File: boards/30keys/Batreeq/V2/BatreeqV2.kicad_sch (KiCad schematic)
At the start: 103 parts, among them J1 Conn_01x12_Female, J2 Conn_01x12_Female, SW1 SW_Push, SW10 SW_Push, SW11 SW_Push, SW12 SW_Push, SW13 SW_Push, SW14 SW_Push, SW15 SW_Push, SW16 SW_Push, SW17 SW_Push, SW18 SW_Push, SW19 SW_Push, SW2 SW_Push, SW20 SW_Push, SW21 SW_Push, SW22 SW_Push, SW23 SW_Push, SW24 SW_Push, SW25 SW_Push, SW26 SW_Push, SW27 SW_Push, SW28 SW_Push, SW29 SW_Push, SW3 SW_Push, SW30 SW_Push, SW31 SW_Push, SW32 SW_Push, SW33 SW_Push, SW34 SW_Push, SW35 SW_Push, SW36 RotaryEncoder, SW37 SW_SPDT, SW4 SW_Push, SW5 SW_Push, SW6 SW_Push, SW7 SW_Push, SW8 SW_Push, SW9 SW_Push, U1 Elite-C, U2 74HC595, U3 TCR2EF19,LM(CT, U4 PMW3360DM-T2QU, U5 DRV2605L

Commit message: batreeqv2
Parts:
- added C6: 4u7, Capacitor_SMD:C_0402_1005Metric, symbol Device:C
- added D40: B5817WS, josh-passives-smt:D_SOD-323, symbol Device:D_Schottky
- added D41, D42, D43, D44, D45, D46, D47, D48, D49, D50, D51, D52, D53, D54, D55, D56, D57, D58, D59, D60, D61, D62, D63, D64, D65, D66, D67, D68, D69, D70, D71, D72, D73, D74: SK6812MINI-E, Alaa:MX_SK6812MINI-E_REV, symbol kicad-keyboard-parts:SK6812MINI-E
- added F1: 500mA, josh-passives-smt:Fuse_0603_1608Metric, symbol Device:Polyfuse_Small
- added J4: Conn_01x08_Female, Alaa:3JST_BAT, symbol Connector:Conn_01x03_Female
- added JP1, JP2, JP3, JP4, JP5, JP6: Jumper_2_Open, Jumper:SolderJumper-2_P1.3mm_Open_TrianglePad1.0x1.5mm, symbol Jumper:Jumper_2_Open
- added U6: 74LVC1T45, josh-soic-sot-etc:SOT-563, symbol Logic_LevelTranslator:SN74LVC1T45DRL
- D1, D10, D11, D12, D13, D14, D15, D16, D17, D18, D19, D2, D20, D21, D22, D23, D24, D25, D26, D27, D28, D29, D3, D30, D31, D32, D33, D34, D35, D36, D37, D38, D39, D4, D5, D6, D7, D8, D9: LCSC C909967 -> C8598
- J3: value (none) -> Conn_01x08_Female; footprint (none) -> Connector_JST:JST_PH_S8B-PH-K_1x08_P2.00mm_Horizontal
- SW1, SW10, SW11, SW12, SW13, SW14, SW15, SW16, SW17, SW18, SW19, SW2, SW20, SW21, SW22, SW23, SW24, SW25, SW26, SW27, SW28, SW29, SW3, SW30, SW31, SW32, SW33, SW34, SW4, SW5, SW6, SW7, SW8, SW9: footprint Alaa:Kailh_hotswap_MX-CHOC-connected -> Alaa:Kailh_hotswap_only_MX-CHOC
- U1: value Elite-C -> (none); footprint Alaa:Elite-C-N!N -> (none); symbol alaa:Elite-C -> alaa:Helios_SeaPicro
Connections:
- net GND: now also C6.2, D41.3 (VSS), D42.3 (VSS), D43.3 (VSS), D44.3 (VSS), D45.3 (VSS), D46.3 (VSS), D47.3 (VSS), D48.3 (VSS), D49.3 (VSS), D50.3 (VSS), D51.3 (VSS), D52.3 (VSS), D53.3 (VSS), D54.3 (VSS), D55.3 (VSS), D56.3 (VSS), D57.3 (VSS), D58.3 (VSS), D59.3 (VSS), D60.3 (VSS), D61.3 (VSS), D62.3 (VSS), D63.3 (VSS), D64.3 (VSS), D65.3 (VSS), D66.3 (VSS), D67.3 (VSS), D68.3 (VSS), D69.3 (VSS), D70.3 (VSS), D71.3 (VSS), D72.3 (VSS), D73.3 (VSS), D74.3 (VSS), J4.2 (Pin_2), U6.2 (GND)
- net RAW: now also JP2.1 (A), JP5.1 (A), U6.6 (VCCB)
- net TFT_DC: now also U1.27 (C7); no longer U1.18 (A1/PF6)
- net VCC: now also JP1.1 (A), U6.1 (VCCA), U6.5 (DIR)
- net bat+: now also J4.1 (Pin_1), J4.3 (Pin_3)
- new net: D62.2 (DOUT), D67.4 (DIN)
- new net: D56.2 (DOUT), D62.4 (DIN)
- new net: D46.2 (DOUT), D52.4 (DIN)
- new net: D46.4 (DIN), D73.2 (DOUT)
- new net: D42.4 (DIN), D71.2 (DOUT)
- new net: D66.2 (DOUT), D71.4 (DIN)
- new net: D58.2 (DOUT), D64.4 (DIN)
- new net: D52.2 (DOUT), D58.4 (DIN)
- new net: JP6.2 (B), U6.3 (A)
- new net: D41.2 (DOUT), D47.4 (DIN)
- new net: D41.4 (DIN), D70.2 (DOUT)
- new net: D68.2 (DOUT), D73.4 (DIN)
- new net: D50.2 (DOUT), D56.4 (DIN)
- new net: D43.2 (DOUT), D49.4 (DIN)
- new net: D43.4 (DIN), D74.2 (DOUT)
- new net: D53.2 (DOUT), D59.4 (DIN)
- new net: D47.2 (DOUT), D53.4 (DIN)
- new net: D61.2 (DOUT), D66.4 (DIN)
- new net: C6.1, F1.2, JP5.2 (B)
- new net: D63.2 (DOUT), D68.4 (DIN)
- new net: D57.2 (DOUT), D63.4 (DIN)
- new net: D49.2 (DOUT), D55.4 (DIN)
- new net: D44.2 (DOUT), D50.4 (DIN)
- new net: D51.2 (DOUT), D57.4 (DIN)
- new net: D40.2 (A), F1.1
- new net: D69.2 (DOUT), D74.4 (DIN)
- new net: D64.2 (DOUT), D69.4 (DIN)
- new net: D48.2 (DOUT), D54.4 (DIN)
- new net: D42.2 (DOUT), D48.4 (DIN)
- new net: D65.2 (DOUT), D70.4 (DIN)
- new net: D55.2 (DOUT), D61.4 (DIN)
- new net: D60.2 (DOUT), D65.4 (DIN)
- new net: D54.2 (DOUT), D60.4 (DIN)
- new net: D67.2 (DOUT), D72.4 (DIN)
- new net: D45.2 (DOUT), D51.4 (DIN)
- new net: D45.4 (DIN), D72.2 (DOUT)
- new net LED_3V3: JP3.1 (A), JP6.1 (A), U1.18 (A1/PF6)
- new net LED_5V: JP4.1 (A), U1.30 (RGB)
- new net LED_DO: D44.4 (DIN), JP3.2 (B), JP4.2 (B), U6.4 (B)
- new net LED_PWR: D40.1 (K), D41.1 (VDD), D42.1 (VDD), D43.1 (VDD), D44.1 (VDD), D45.1 (VDD), D46.1 (VDD), D47.1 (VDD), D48.1 (VDD), D49.1 (VDD), D50.1 (VDD), D51.1 (VDD), D52.1 (VDD), D53.1 (VDD), D54.1 (VDD), D55.1 (VDD), D56.1 (VDD), D57.1 (VDD), D58.1 (VDD), D59.1 (VDD), D60.1 (VDD), D61.1 (VDD), D62.1 (VDD), D63.1 (VDD), D64.1 (VDD), D65.1 (VDD), D66.1 (VDD), D67.1 (VDD), D68.1 (VDD), D69.1 (VDD), D70.1 (VDD), D71.1 (VDD), D72.1 (VDD), D73.1 (VDD), D74.1 (VDD), JP1.2 (B), JP2.2 (B)
- no-connect marks 15 -> 14
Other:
- note added: "3v3 -> 5V logic shift"
- note added: "WS2812 Driver"
- moved on the sheet: D35, D36, D37, D38, D39, HAT1, SW35, SW37

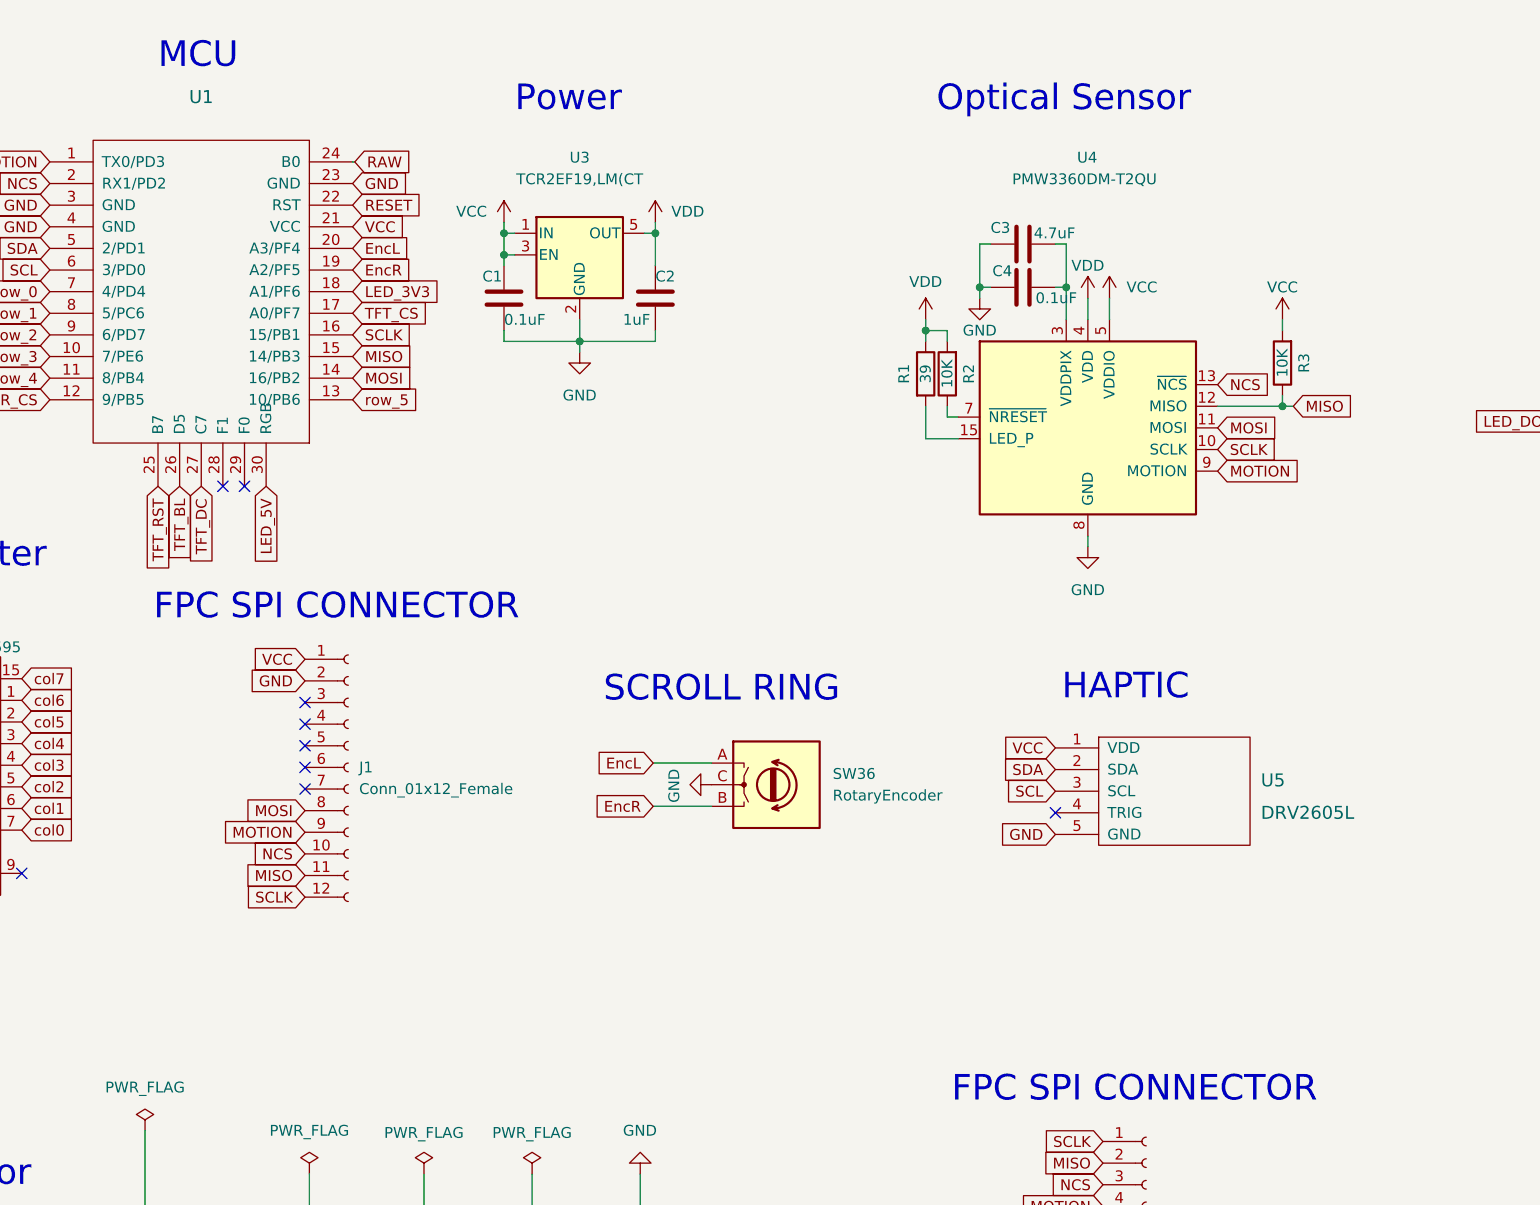
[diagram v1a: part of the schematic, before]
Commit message: add resistors to scroll ring circuit
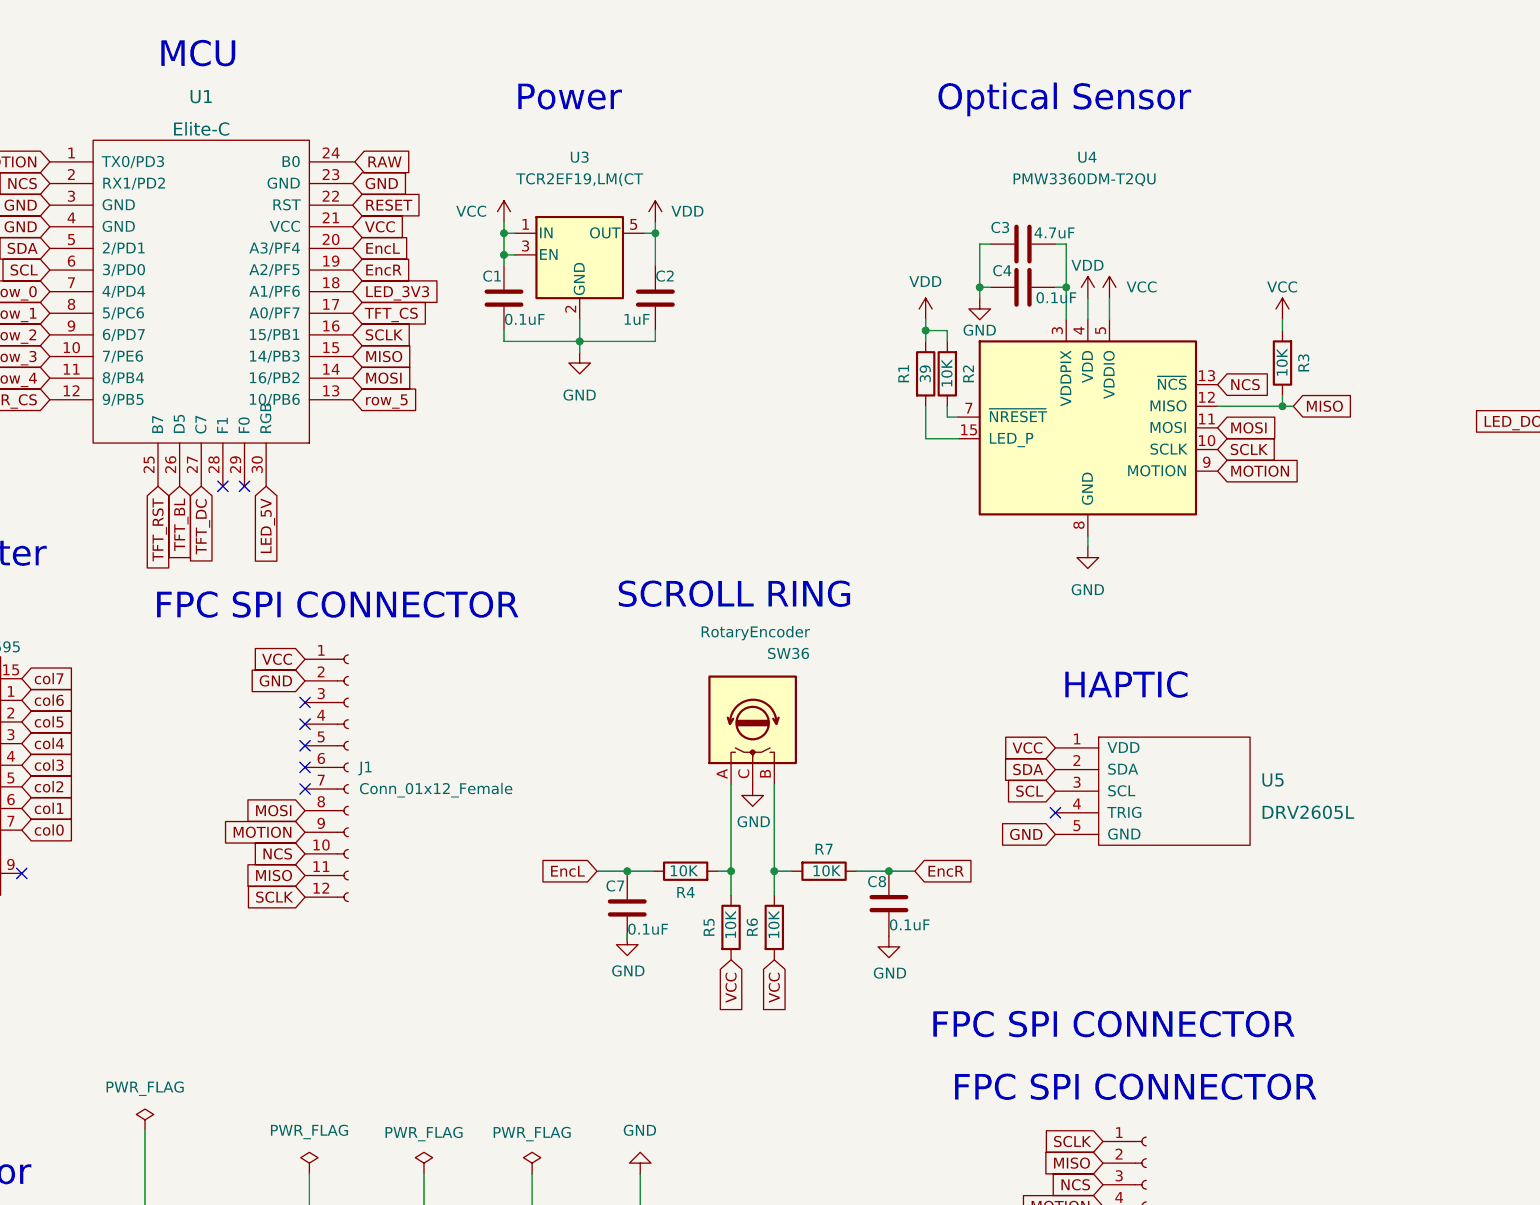
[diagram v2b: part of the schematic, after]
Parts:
- added C7, C8: 0.1uF, Capacitor_SMD:C_0805_2012Metric, symbol Device:C
- added R4, R5, R6, R7: 10K, Resistor_SMD:R_0805_2012Metric, symbol Device:R
- U1: value (none) -> Elite-C; footprint (none) -> Alaa:Helios-SeaPicro-Nano
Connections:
- net EncL: now also C7.1, R4.1; no longer SW36.A
- net EncR: now also C8.1, R7.1; no longer SW36.B
- net GND: now also C7.2, C8.2
- net VCC: now also R5.2, R6.2
- new net: R4.2, R5.1, SW36.A
- new net: R6.1, R7.2, SW36.B
